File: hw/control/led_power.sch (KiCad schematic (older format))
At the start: 25 parts, among them Q1001 BC807, Q1002 BC817, U801 LM2678T-ADJ

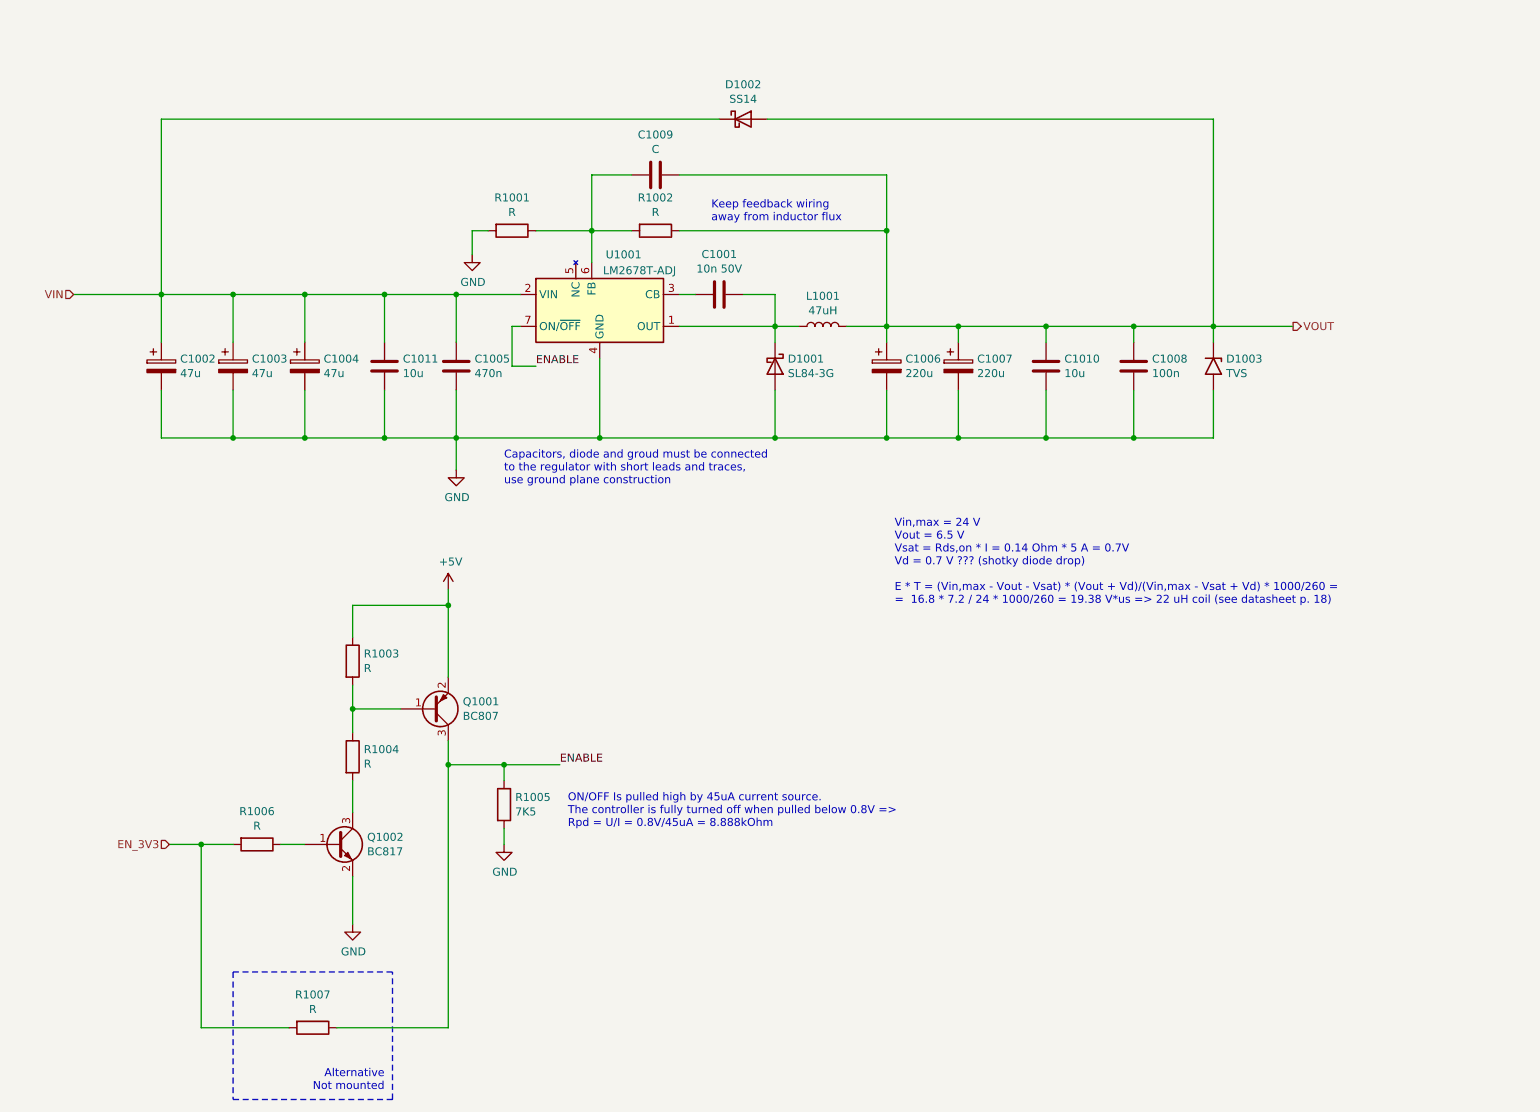
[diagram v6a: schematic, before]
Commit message: [hw] Move LED power enable to its own sheet
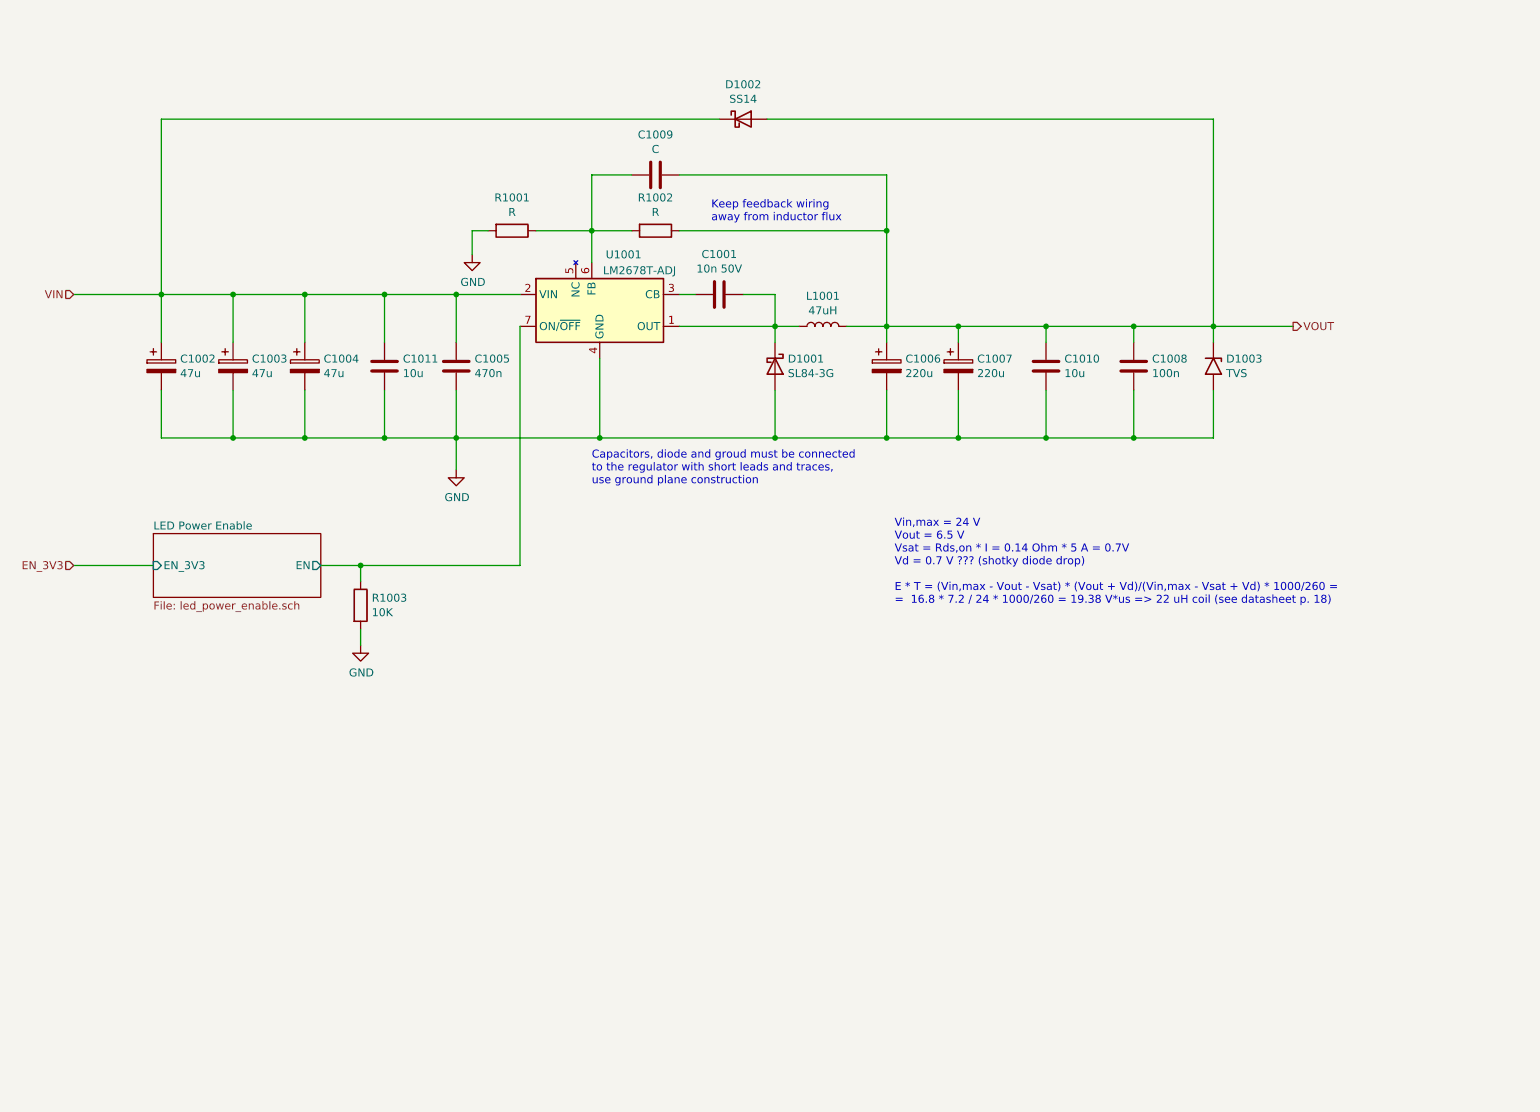
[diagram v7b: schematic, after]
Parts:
- removed Q1001: BC807, Package_TO_SOT_SMD:SOT-23_Handsoldering, symbol Device:Q_PNP_BEC
- removed Q1002: BC817, Package_TO_SOT_SMD:SOT-23_Handsoldering, symbol Device:Q_NPN_BEC
- removed R1004, R1006, R1007: R, Resistor_SMD:R_0805_2012Metric_Pad1.20x1.40mm_HandSolder, symbol Device:R
- removed R1005: 7K5, Resistor_SMD:R_0805_2012Metric_Pad1.20x1.40mm_HandSolder, symbol Device:R
- R1003: value R -> 10K
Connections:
- net ENABLE is gone; now on net LED Power Enable/EN: U801.7 (ON/~OFF~)
- net GND: now also R1003.2
- net +5V renamed LED Power Enable/EN
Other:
- note removed: "Alternative\nNot mounted"
- note removed: "ON/OFF Is pulled high by 45uA current source.\nThe controller is fully turned off when pulled below 0.8V =>\nRpd = U/I = 0.8V/45uA = 8.888kOhm"
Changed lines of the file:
@@
 $Descr A4 11693 8268
 encoding utf-8
-Sheet 8 13
+Sheet 11 15
 Title "WS2812 Controller"
 Date "2021-10-10"
@@
 Text HLabel 2100 2300 0    50   Input ~ 0
 VIN
-Text HLabel 2700 5750 0    50   Input ~ 0
-EN_3V3
 Text HLabel 9750 2500 2    50   Output ~ 0
 VOUT
@@
 Text Notes 6100 1850 0    50   ~ 0
 Keep feedback wiring\naway from inductor flux
-Text Notes 4800 3500 0    50   ~ 0
+Text Notes 5350 3500 0    50   ~ 0
 Capacitors, diode and groud must be connected\nto the regulator with short leads and traces,\nuse ground plane construction
-$Comp
-L Device:R R1006
-U 1 1 6147DB7E
-P 3250 5750
-AR Path="/614AE8DA/6147DB7E" Ref="R1006"  Part="1"
-AR Path="/614AB031/6147DB7E" Ref="R806"  Part="1"
-F 0 "R1006" V 3043 5750 50  0000 C CNN
-F 1 "R" V 3134 5750 50  0000 C CNN
-F 2 "Resistor_SMD:R_0805_2012Metric_Pad1.20x1.40mm_HandSolder" V 3180 5750 50  0001 C CNN
-F 3 "~" H 3250 5750 50  0001 C CNN
-	1    3250 5750
-	0    1    1    0
-$EndComp
-$Comp
-L Device:Q_NPN_BEC Q1002
-U 1 1 6147EFCD
-P 3750 5750
-AR Path="/614AE8DA/6147EFCD" Ref="Q1002"  Part="1"
-AR Path="/614AB031/6147EFCD" Ref="Q802"  Part="1"
-F 0 "Q1002" H 3941 5796 50  0000 L CNN
-F 1 "BC817" H 3941 5705 50  0000 L CNN
-F 2 "Package_TO_SOT_SMD:SOT-23_Handsoldering" H 3950 5850 50  0001 C CNN
-F 3 "~" H 3750 5750 50  0001 C CNN
-	1    3750 5750
-	1    0    0    -1
-$EndComp
-Wire Wire Line
-	3400 5750 3550 5750
-$Comp
-L Device:Q_PNP_BEC Q1001
-U 1 1 61480A0D
-P 4350 4900
-AR Path="/614AE8DA/61480A0D" Ref="Q1001"  Part="1"
-AR Path="/614AB031/61480A0D" Ref="Q801"  Part="1"
-F 0 "Q1001" H 4541 4854 50  0000 L CNN
-F 1 "BC807" H 4541 4945 50  0000 L CNN
-F 2 "Package_TO_SOT_SMD:SOT-23_Handsoldering" H 4550 5000 50  0001 C CNN
-F 3 "~" H 4350 4900 50  0001 C CNN
-	1    4350 4900
-	1    0    0    1
-$EndComp
-$Comp
-L Device:R R1004
-U 1 1 6148128F
-P 3850 5200
-AR Path="/614AE8DA/6148128F" Ref="R1004"  Part="1"
-AR Path="/614AB031/6148128F" Ref="R804"  Part="1"
-F 0 "R1004" H 3920 5246 50  0000 L CNN
-F 1 "R" H 3920 5155 50  0000 L CNN
-F 2 "Resistor_SMD:R_0805_2012Metric_Pad1.20x1.40mm_HandSolder" V 3780 5200 50  0001 C CNN
-F 3 "~" H 3850 5200 50  0001 C CNN
-	1    3850 5200
-	1    0    0    -1
-$EndComp
-$Comp
-L Device:R R1003
-U 1 1 614817B0
-P 3850 4600
-AR Path="/614AE8DA/614817B0" Ref="R1003"  Part="1"
-AR Path="/614AB031/614817B0" Ref="R803"  Part="1"
-F 0 "R1003" H 3920 4646 50  0000 L CNN
-F 1 "R" H 3920 4555 50  0000 L CNN
-F 2 "Resistor_SMD:R_0805_2012Metric_Pad1.20x1.40mm_HandSolder" V 3780 4600 50  0001 C CNN
-F 3 "~" H 3850 4600 50  0001 C CNN
-	1    3850 4600
-	1    0    0    -1
-$EndComp
-$Comp
-L power:GND #PWR01004
-U 1 1 61483286
-P 3850 6250
-AR Path="/614AE8DA/61483286" Ref="#PWR01004"  Part="1"
-AR Path="/614AB031/61483286" Ref="#PWR0804"  Part="1"
-F 0 "#PWR01004" H 3850 6000 50  0001 C CNN
-F 1 "GND" H 3855 6077 50  0000 C CNN
-F 2 "" H 3850 6250 50  0001 C CNN
-F 3 "" H 3850 6250 50  0001 C CNN
-	1    3850 6250
-	1    0    0    -1
-$EndComp
-Wire Wire Line
-	3850 5550 3850 5350
-Wire Wire Line
-	3850 5050 3850 4900
-$Comp
-L power:+5V #PWR01003
-U 1 1 61486663
-P 4450 4150
-AR Path="/614AE8DA/61486663" Ref="#PWR01003"  Part="1"
-AR Path="/614AB031/61486663" Ref="#PWR0803"  Part="1"
-F 0 "#PWR01003" H 4450 4000 50  0001 C CNN
-F 1 "+5V" H 4465 4323 50  0000 C CNN
-F 2 "" H 4450 4150 50  0001 C CNN
-F 3 "" H 4450 4150 50  0001 C CNN
-	1    4450 4150
-	1    0    0    -1
-$EndComp
-Wire Wire Line
-	4450 4150 4450 4250
-Wire Wire Line
-	3850 4450 3850 4250
-Wire Wire Line
-	3850 4250 4450 4250
-Connection ~ 4450 4250
-Wire Wire Line
-	4450 4250 4450 4700
-Wire Wire Line
-	4150 4900 3850 4900
-Connection ~ 3850 4900
-Wire Wire Line
-	3850 4900 3850 4750
-$Comp
-L Device:R R1005
-U 1 1 6148D73D
-P 4800 5500
-AR Path="/614AE8DA/6148D73D" Ref="R1005"  Part="1"
-AR Path="/614AB031/6148D73D" Ref="R805"  Part="1"
-F 0 "R1005" H 4870 5546 50  0000 L CNN
-F 1 "7K5" H 4870 5455 50  0000 L CNN
-F 2 "Resistor_SMD:R_0805_2012Metric_Pad1.20x1.40mm_HandSolder" V 4730 5500 50  0001 C CNN
-F 3 "~" H 4800 5500 50  0001 C CNN
-	1    4800 5500
-	1    0    0    -1
-$EndComp
-Wire Wire Line
-	4450 5250 4450 5100
-Text Label 5150 5250 0    50   ~ 0
-ENABLE
-Text Label 5000 2750 0    50   ~ 0
-ENABLE
-Wire Wire Line
-	5000 2750 4850 2750
-Wire Wire Line
-	4850 2750 4850 2500
-Wire Wire Line
-	4850 2500 4900 2500
-$Comp
-L Device:R R1007
-U 1 1 614CC1BE
-P 3600 6900
-AR Path="/614AE8DA/614CC1BE" Ref="R1007"  Part="1"
-AR Path="/614AB031/614CC1BE" Ref="R807"  Part="1"
-F 0 "R1007" V 3393 6900 50  0000 C CNN
-F 1 "R" V 3484 6900 50  0000 C CNN
-F 2 "Resistor_SMD:R_0805_2012Metric_Pad1.20x1.40mm_HandSolder" V 3530 6900 50  0001 C CNN
-F 3 "~" H 3600 6900 50  0001 C CNN
-	1    3600 6900
-	0    1    1    0
-$EndComp
-Wire Wire Line
-	3750 6900 4450 6900
-Wire Wire Line
-	4450 6900 4450 5250
-Connection ~ 4450 5250
-Wire Wire Line
-	4450 5250 4800 5250
-Wire Wire Line
-	2700 5750 2900 5750
-Wire Wire Line
-	3450 6900 2900 6900
-Wire Wire Line
-	2900 6900 2900 5750
-Connection ~ 2900 5750
-Wire Wire Line
-	2900 5750 3100 5750
 Text Notes 7250 4250 0    50   ~ 0
 Vin,max = 24 V\nVout = 6.5 V\nVsat = Rds,on * I = 0.14 Ohm * 5 A = 0.7V\nVd = 0.7 V ??? (shotky diode drop)\n\nE * T = (Vin,max - Vout - Vsat) * (Vout + Vd)/(Vin,max - Vsat + Vd) * 1000/260 = \n=  16.8 * 7.2 / 24 * 1000/260 = 19.38 V*us => 22 uH coil (see datasheet p. 18)
@@
 Wire Wire Line
 	8750 3200 8750 2900
-Text Notes 4050 7300 2    50   ~ 0
-Alternative\nNot mounted
-Wire Notes Line
-	3100 6550 3100 7350
-Wire Notes Line
-	3100 7350 4100 7350
-Wire Notes Line
-	4100 7350 4100 6550
-Wire Notes Line
-	4100 6550 3100 6550
 $Comp
 L Device:C C809
@@
 	7200 1900 7200 2500
 Connection ~ 7200 1900
-Text Notes 5200 5650 0    50   ~ 0
-ON/OFF Is pulled high by 45uA current source.\nThe controller is fully turned off when pulled below 0.8V =>\nRpd = U/I = 0.8V/45uA = 8.888kOhm
-$Comp
-L power:GND #PWR0805
-U 1 1 616CF895
-P 4800 5750
-AR Path="/614AB031/616CF895" Ref="#PWR0805"  Part="1"
-AR Path="/614AE8DA/616CF895" Ref="#PWR01005"  Part="1"
-F 0 "#PWR01005" H 4800 5500 50  0001 C CNN
-F 1 "GND" H 4805 5577 50  0000 C CNN
-F 2 "" H 4800 5750 50  0001 C CNN
-F 3 "" H 4800 5750 50  0001 C CNN
-	1    4800 5750
-	1    0    0    -1
-$EndComp
-Wire Wire Line
-	4800 5350 4800 5250
-Connection ~ 4800 5250
-Wire Wire Line
-	4800 5250 5150 5250
-Wire Wire Line
-	4800 5750 4800 5650
-Wire Wire Line
-	3850 5950 3850 6250
 $Comp
 L Device:C C810
@@
 Wire Wire Line
 	2650 1200 6150 1200
+$Sheet
+S 2600 3800 1050 400
+U 618915A5
+F0 "LED Power Enable" 50
+F1 "led_power_enable.sch" 50
+F2 "EN_3V3" I L 2600 4000 50
+F3 "EN" O R 3650 4000 50
+$EndSheet
+Wire Wire Line
+	4900 4000 3900 4000
+Text HLabel 2100 4000 0    50   Input ~ 0
+EN_3V3
+Wire Wire Line
+	2100 4000 2600 4000
+Wire Wire Line
+	4900 2500 4900 4000
+$Comp
+L power:GND #PWR0803
+U 1 1 618AFCCB
+P 3900 4500
+AR Path="/614AB031/618AFCCB" Ref="#PWR0803"  Part="1"
+AR Path="/614AE8DA/618AFCCB" Ref="#PWR01104"  Part="1"
+AR Path="/614AB031/618915A5/618AFCCB" Ref="#PWR?"  Part="1"
+AR Path="/614AE8DA/618915A5/618AFCCB" Ref="#PWR?"  Part="1"
+F 0 "#PWR01104" H 3900 4250 50  0001 C CNN
+F 1 "GND" H 3905 4327 50  0000 C CNN
+F 2 "" H 3900 4500 50  0001 C CNN
+F 3 "" H 3900 4500 50  0001 C CNN
+	1    3900 4500
+	1    0    0    -1
+$EndComp
+Wire Wire Line
+	3900 4500 3900 4400
+Wire Wire Line
+	3900 4100 3900 4000
+Connection ~ 3900 4000
+Wire Wire Line
+	3900 4000 3650 4000
+$Comp
+L Device:R R1003
+U 1 1 618C0BB7
+P 3900 4250
+AR Path="/614AE8DA/618C0BB7" Ref="R1003"  Part="1"
+AR Path="/614AB031/618C0BB7" Ref="R803"  Part="1"
+F 0 "R1003" H 3970 4296 50  0000 L CNN
+F 1 "10K" H 3970 4205 50  0000 L CNN
+F 2 "Resistor_SMD:R_0805_2012Metric_Pad1.20x1.40mm_HandSolder" V 3830 4250 50  0001 C CNN
+F 3 "~" H 3900 4250 50  0001 C CNN
+	1    3900 4250
+	1    0    0    -1
+$EndComp
 $EndSCHEMATC

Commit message: [hw] Re-annotate all components
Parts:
- renumbered C1002 to C1103, C1003 to C1104, C1004 to C1105, C1005 to C1107, C1006 to C1108, C1007 to C1109, C809 to C801, C801 to C802, C811 to C806, C808 to C811, D1001 to D1102, D802 to D801, L1001 to L1101, R1001 to R1101, R1002 to R1102, R1003 to R1103
